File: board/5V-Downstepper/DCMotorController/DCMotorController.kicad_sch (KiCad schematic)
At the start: 21 parts, among them U1 TPS54360DDA

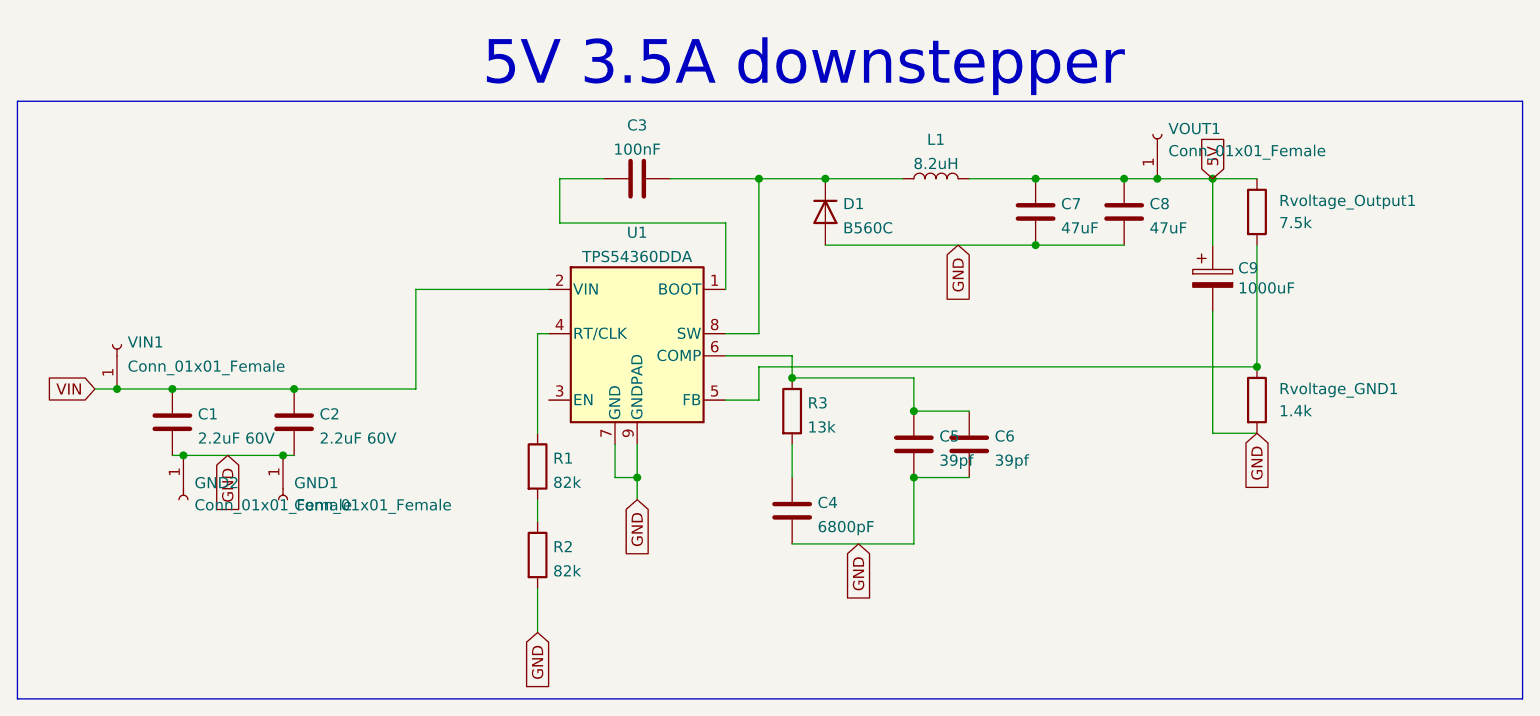
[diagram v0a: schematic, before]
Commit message: adjusted voltage divider for tps
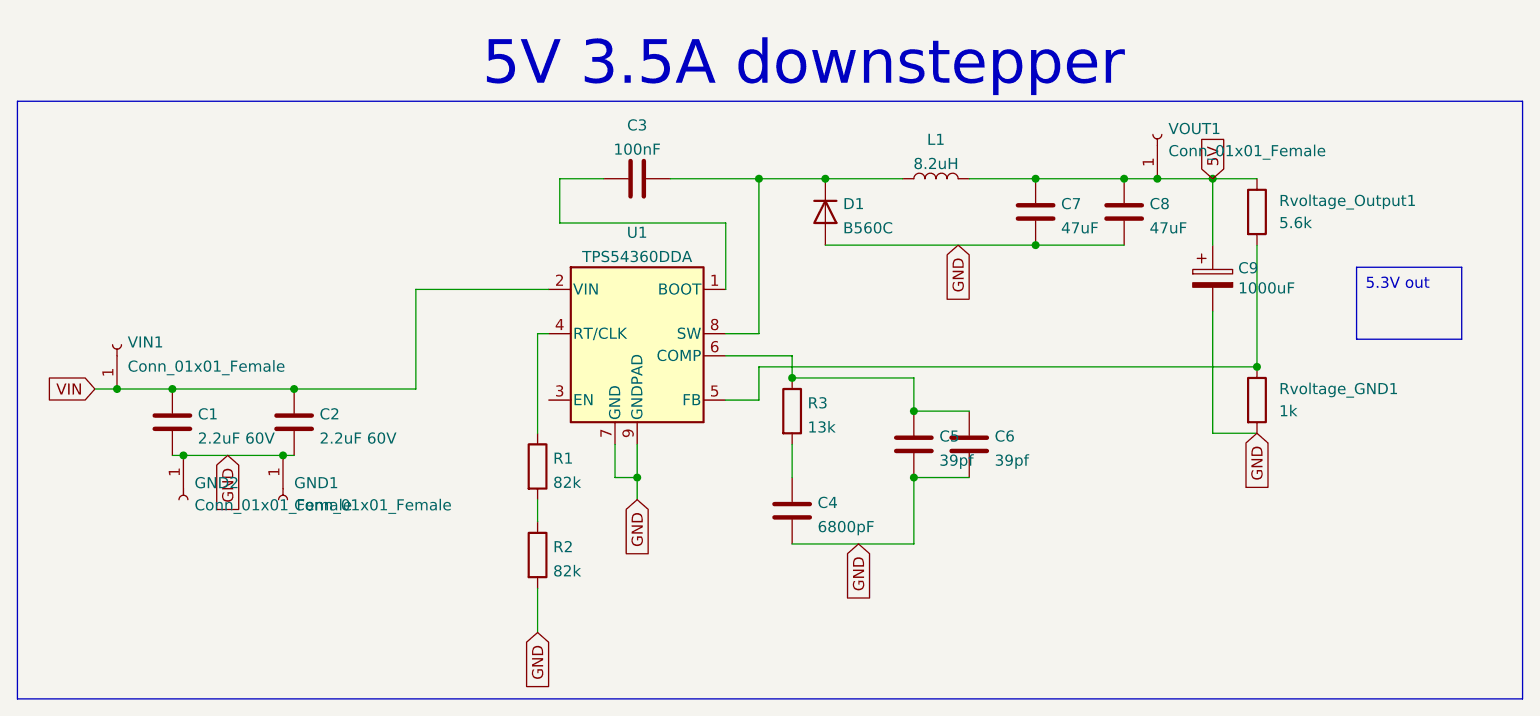
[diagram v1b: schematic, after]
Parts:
- Rvoltage_GND1: value 1.4k -> 1k
- Rvoltage_Output1: value 7.5k -> 5.6k
